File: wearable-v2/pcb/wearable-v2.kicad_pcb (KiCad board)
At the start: 2 copper layers, 89 parts, among them IC1 TESEO-LIV3F, J7 USB_C_Receptacle_USB2.0, SW1 SW_Push, U1 DT1446-04V, U10 ATmega328PB-M, U11 TMP1075, U12 MAX30102, U14 LIS2DE12, U2 MCP73832-2-OT, U3 TCA6408A, U4 FT201XQ, U6 BC833, U7 MX25R8035FZxxx0, U8 PCF85063ATL, U9 APDS-9250, Y1 32.768kHz

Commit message: Standard connector almost complete
Added JLCPCB manufacturer settings to PCB
Ensured all components are available and Tape and Reel with smallest footprint available
Signed-off-by: Adam Fowler <adam@adamfowler.org>
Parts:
- removed C22, C23: 1uF, Capacitor_SMD:C_0402_1005Metric
- removed C3: 4.7uF, Capacitor_SMD:C_0402_1005Metric
- removed the C6 at (115.1, 116.8)
- removed C7: 10uF, Capacitor_SMD:C_0402_1005Metric
- removed R3: 0, Resistor_SMD:R_0603_1608Metric
- removed TP4: VDD, TestPoint:TestPoint_Pad_D1.0mm
- U2: value MCP73832-2-OT -> MCP73831/2-2MC; footprint Package_TO_SOT_SMD:SOT-23-5 -> Package_DFN_QFN:DFN-8-1EP_3x2mm_P0.5mm_EP1.75x1.45mm
- moved H1 49.9 mm to (63.4, 40.1)
- moved SW1 46.9 mm to (58.8, 150.7), turned to 90 degrees
- moved C29 34.1 mm to (220.0, 84.9)
- moved TP18 34.1 mm to (229.1, 68.9)
- moved U14 34.1 mm to (222.8, 71.2)
- moved C27 34.1 mm to (219.5, 77.4)
- moved C28 34.1 mm to (222.3, 80.1)
- moved R7 34.1 mm to (221.8, 67.9)
- moved TP17 34.1 mm to (226.8, 76.3)
- moved R15 26.4 mm to (28.6, 126.6)
- moved C14 26.4 mm to (28.5, 122.8)
- moved U9 26.4 mm to (28.6, 124.7)
- moved C2 25.3 mm to (104.8, 131.3)
- moved C1 22.5 mm to (104.8, 132.3)
- moved U1 7.46 mm to (104.9, 135.8), turned to 90 degrees
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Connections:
- C10 pad 1: VDD1 -> VDD
- C11 pad 1: VDD1 -> VDD
- C12 pad 2: VDD1 -> VDD
- C13 pad 1: VDD1 -> VDD
- C24 pad 1: VDD1 -> VDD
- C30 pad 2: VDD1 -> VDD
- C6 pad 1: VDD1 -> VDD
- D2 pad 1: VDD1 -> VDD
- IC1 pad 14: VDD1 -> VDD
- IC1 pad 6: VDD1 -> VDD
- IC1 pad 7: VDD1 -> VDD
- IC1 pad 8: VDD1 -> VDD
- R1 pad 1: Net-(U2-PROG) -> GND
- R1 pad 2: GND -> Net-(U2-PROG)
- R10 pad 1: VDD1 -> VDD
- R11 pad 1: VDD1 -> VDD
- R16 pad 1: VDD1 -> VDD
- TP12 pad 1: VDD1 -> VDD
- U10 pad 18: VDD1 -> VDD
- U10 pad 4: VDD1 -> VDD
- U15 pad 11: (no net) -> GND
- U15 pad 8: VDD1 -> VDD
- U2 pad 1: /Standard Connector/CH_STAT -> VBUS
- U2 pad 2: GND -> VBUS
- U2 pad 4: VBUS -> +BATT
- U2 pad 5: Net-(U2-PROG) -> /Standard Connector/CH_STAT
- U3 pad 1: VDD1 -> VDD
- U3 pad 16: VDD1 -> VDD
- U3 pad 2: VDD1 -> VDD
- U4 pad 10: VDD1 -> VDD
- U6 pad 1: VDD1 -> VDD
- U7 pad 8: VDD1 -> VDD
- U8 pad 10: VDD1 -> VDD
- U8 pad EP: unconnected-(U8-PadEP) -> GND
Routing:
- net GND: track 35.6 -> 128.7 mm, vias 9 -> 17
- net VDD: track 0.00 -> 81.5 mm, vias 5 -> 6
- net +1V8: track 20.4 -> 70.8 mm, vias 0 -> 1
- net /Bio Board V1/SCL: track 44.4 -> 69.4 mm, vias 4 -> 5
- net VBUS: track 12.0 -> 32.0 mm, vias 0 -> 2
- net /Standard Connector/USB_D-: track 8.76 -> 23.0 mm, vias 2 -> 4
- net /Bio Board V1/SDA: track 58.2 -> 72.4 mm, vias 2 -> 7
- net /Standard Connector/USB_D+: track 3.99 -> 16.6 mm, vias 0 -> 2
- net /Compute - Fanstel BC833M - Nordic Semi nRF52833 based/LED_B: track 12.7 -> 3.08 mm
- net +BATT: track 25.1 -> 16.6 mm, vias 0 -> 2
- net VDD1: track 8.06 -> 0.00 mm
- net /Standard Connector/CH_STAT: track 7.48 -> 1.86 mm
- net /Compute - Fanstel BC833M - Nordic Semi nRF52833 based/SWDCLK: track 24.5 -> 21.0 mm
- net /Compute - Fanstel BC833M - Nordic Semi nRF52833 based/SWDIO: track 23.6 -> 21.4 mm
- net /Compute - Fanstel BC833M - Nordic Semi nRF52833 based/NFC2: track 8.72 -> 10.5 mm
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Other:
- board outline added: 247 x 147.3 mm
- board text added: "EXT 1 CPU TOP/CENTRAL"
- board text added: "EXT 1 CPU TOP/CENTRAL NB Components point DOWN (Toward Skin)"
- board text added: "EXT 2 BIO BOTTOM+SKIN"
- board text added: "EXT 3 GNSS/5G TOP/CENTRAL"
- board text added: "EXT 4 DISPLAY + FEEDBACK BOTTOM"
- board text added: "FRONT 1 LIGHT SENSOR TOP LEFT"
- board text added: "FRONT 2 GNSS ANTENNA TOP RIGHT"
- board text added: "FRONT 3 LEFT BUTTON BUTTOM LEFT"
- board text added: "FRONT 4 RIGHT BUTTON BUTTOM RIGHT"
- board text added: "TODO check USB-C D+ and D- and see if we need to connect both"
- board text removed: "8x40mm"
- board text removed: "Bio Board Here"
- board text removed: "Compute Board Here"
- board text removed: "Display Board Here"
- board text removed: "Front Button Panel"
- board text removed: "Front Light Sensor Panel"
- board text removed: "Positioning Board Here"

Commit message: Completed individual board layouts
Signed-off-by: Adam Fowler <adam@adamfowler.org>
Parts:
- TP10, TP11, TP8, U12: moved to B.Cu
- moved C21 193.7 mm to (215.9, 113.7), turned to 180 degrees
- moved C19 193.2 mm to (207.4, 106.5)
- moved C20 193.2 mm to (208.6, 106.5)
- moved U11 193.2 mm to (205.1, 106.8)
- moved C18 192.8 mm to (215.9, 112.7), turned to 180 degrees
- moved C17 191.8 mm to (216.0, 111.7), turned to 180 degrees
- moved U12 191.8 mm to (212.0, 111.7), turned to 180 degrees
- moved TP8 190.8 mm to (199.4, 107.0), turned to 180 degrees
- moved TP10 189.4 mm to (205.1, 112.3), turned to 180 degrees
- moved TP11 185.9 mm to (212.2, 107.4), turned to 180 degrees
- moved H1 166.4 mm to (218.2, 101.1)
- moved TP16 152.3 mm to (162.8, 124.1)
- moved TP15 140.8 mm to (160.3, 124.1)
- moved TP12 140.2 mm to (170.4, 124.1)
- moved TP13 139.7 mm to (167.9, 124.1)
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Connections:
- ANT1 pad 2: (no net) -> GND
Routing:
- net GND: track 128.7 -> 237.3 mm, vias 17 -> 20
- net /Bio Board V1/SDA: track 72.4 -> 143.3 mm, vias 7 -> 14
- net VDD: track 81.5 -> 151.7 mm, vias 6 -> 16
- net /Bio Board V1/SCL: track 69.4 -> 135.8 mm, vias 5 -> 11
- net /Positioning Board V1/GNSS_INT: track 0.00 -> 30.8 mm
- net /Positioning Board V1/POS_RESETn: track 0.00 -> 26.7 mm, vias 0 -> 2
- net /Compute - Fanstel BC833M - Nordic Semi nRF52833 based/EXT_INT1: track 0.00 -> 24.2 mm
- net +1V8: track 70.8 -> 87.2 mm, vias 1 -> 4
- net /Bio Board V1/BIO_INT: track 17.2 -> 3.34 mm
- net /Positioning Board V1/ANT_RF: track 0.00 -> 13.3 mm
- net Net-(ANT1-Pad1): track 0.00 -> 10.8 mm
- net /Positioning Board V1/ACC_INT1: track 0.00 -> 8.62 mm
- net /Positioning Board V1/ACC_INT2: track 0.00 -> 7.77 mm
- net Net-(U14-~{CS}): track 0.00 -> 3.78 mm
- net /Bio Board V1/TMP_INT: track 2.23 -> 4.87 mm, vias 0 -> 1
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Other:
- board size 247 x 147.3 mm -> 202.8 x 42.4 mm
- board text added: "EXT 1 COMPUTE TOP/CENTRAL NB Components point DOWN (Toward Skin) NB Connector points DOWN (Toward Skin and Connector board)"
- board text added: "EXT 2 BIO BOTTOM+SKIN NB Components point UP (Toward Connector) except Bio sensors which point DOWN (Toward skin) NB Connector points UP (Away from skin, toward Connector board)"
- board text added: "EXT 3 POSITIONING (GNSS), OR 5G, ETC. TOP/CENTRAL NB Components point DOWN (Toward Skin) NB Connector points DOWN (Toward Skin and Connector board)"
- board text added: "EXT 4 DISPLAY + FEEDBACK BOTTOM NB Components point UP (Toward Connector) Nothing points DOWN (Toward skin) NB Connector points UP (Away from skin, toward Connector board) NB ZIF connector extends out the bottom of this board and wraps around the top boards, then the battery, to connect to the display"
- board text removed: "35x19mm"
- board text removed: "ANT"
- board text removed: "Deleted???"
- board text removed: "EXT 1 CPU TOP/CENTRAL NB Components point DOWN (Toward Skin)"
- board text removed: "GNSS"
- board text removed: "TODO check USB-C D+ and D- and see if we need to connect both"
- board text removed: "TODO verify manufacturer track width minimums"

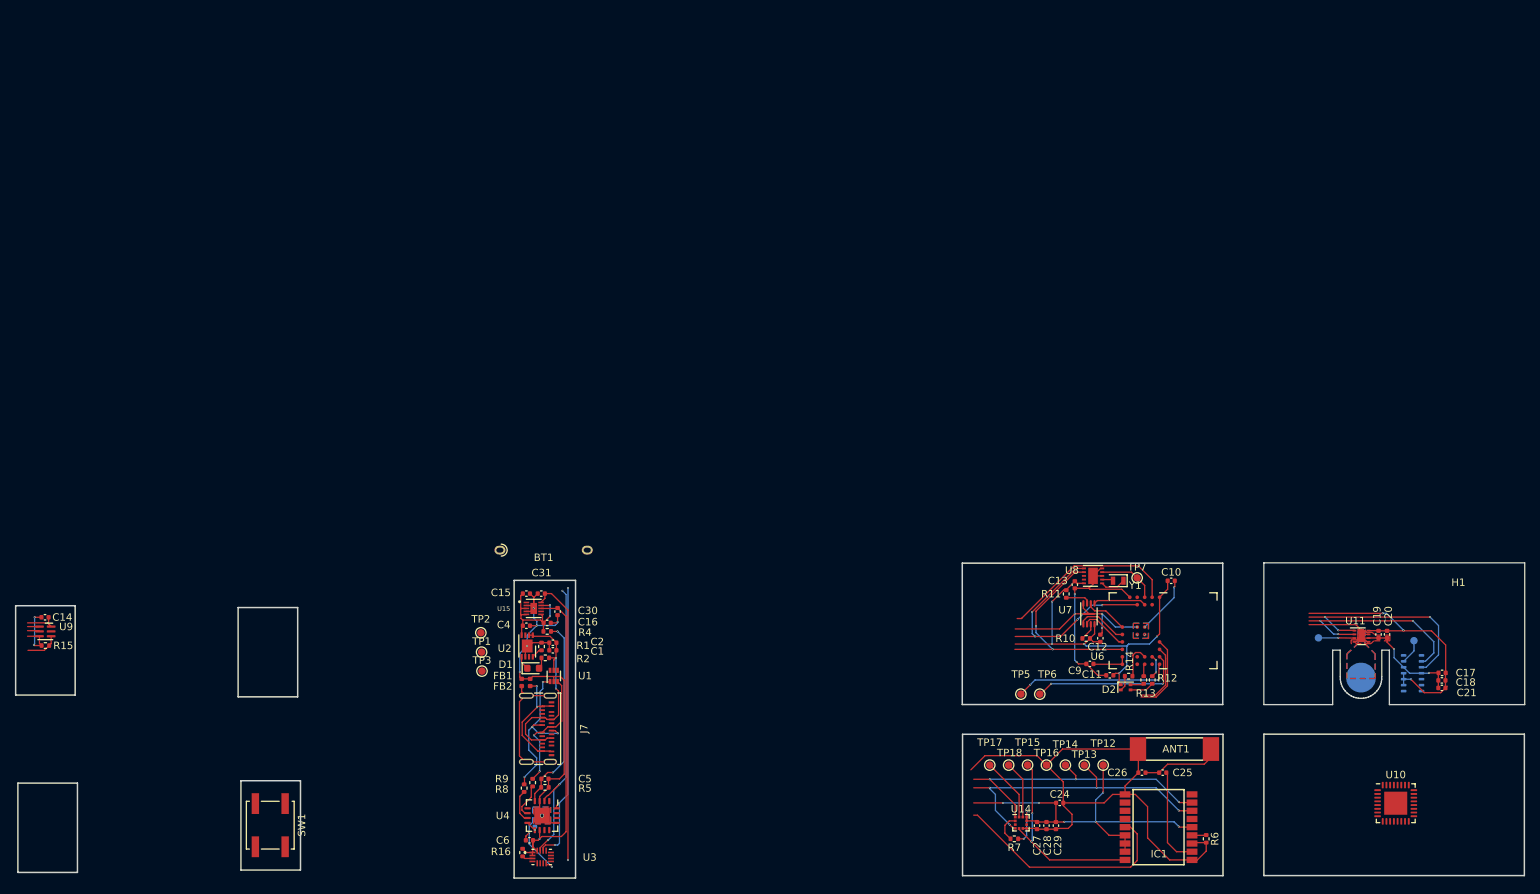
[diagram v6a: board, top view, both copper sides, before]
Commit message: Laid out all boards together
Added missing models for oscillator, push button, daylight sensor
Signed-off-by: Adam Fowler <adam@adamfowler.org>
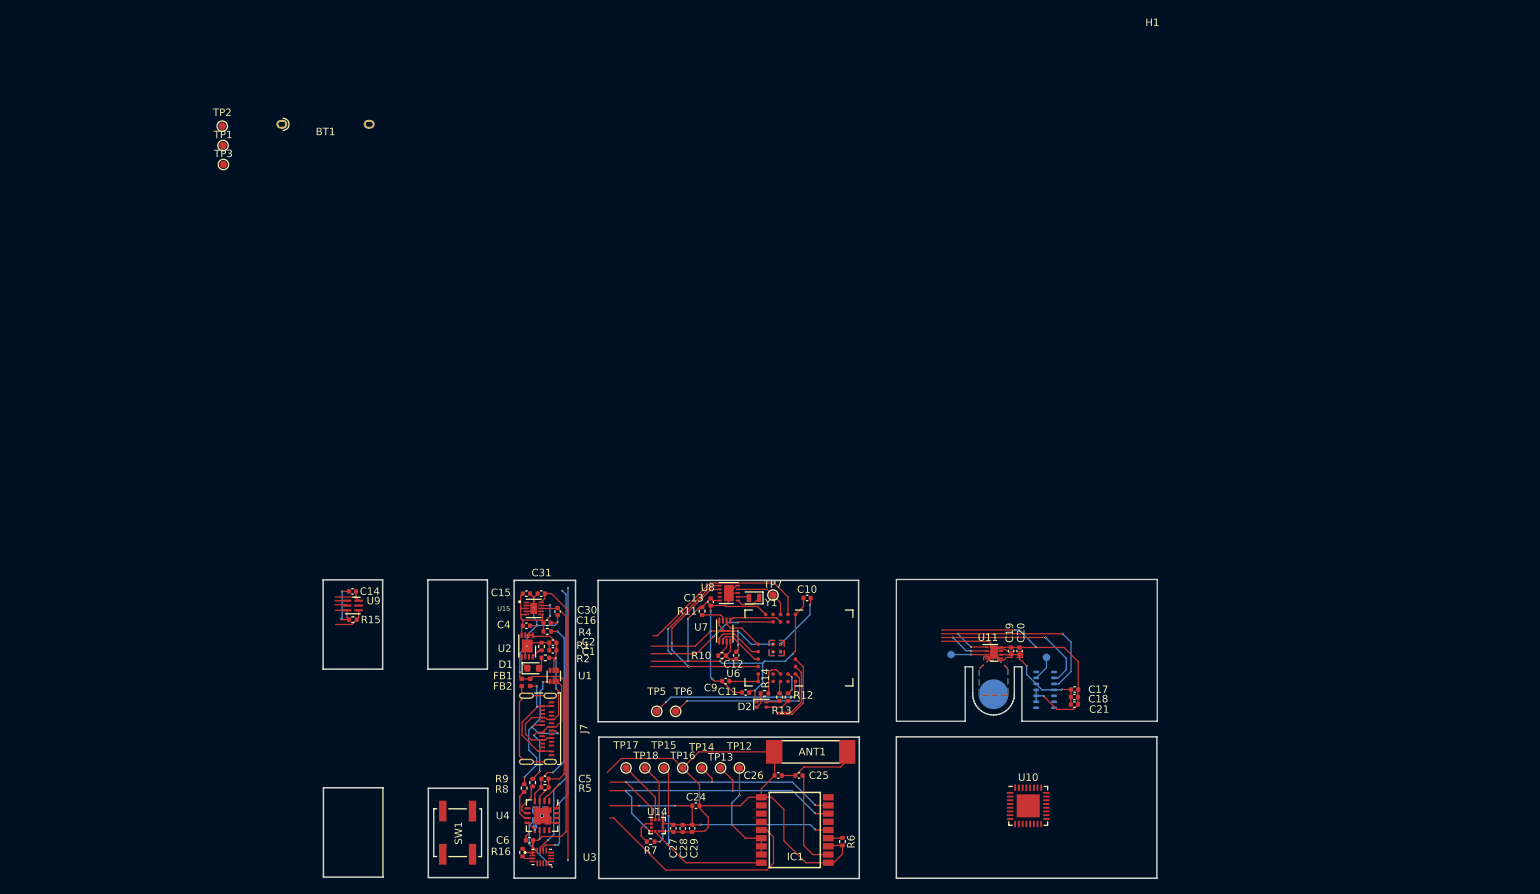
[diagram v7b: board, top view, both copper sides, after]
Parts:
- moved H1 85.7 mm to (177.0, 25.9)
- moved TP1 76.4 mm to (52.2, 40.8)
- moved TP2 76.4 mm to (52.1, 38.2)
- moved TP3 76.4 mm to (52.2, 43.4)
- moved BT1 64.3 mm to (65.9, 38.0)
- moved C17 49.4 mm to (166.6, 113.9)
- moved C19 49.4 mm to (158.1, 108.8)
- moved C20 49.4 mm to (159.2, 108.8)
- moved TP10 49.4 mm to (155.7, 114.6)
- moved TP11 49.4 mm to (162.8, 109.6)
- moved TP8 49.4 mm to (150.0, 109.2)
- moved U11 49.4 mm to (155.8, 109.0)
- moved U12 49.4 mm to (162.6, 114.0)
- moved C18 49.4 mm to (166.6, 114.9)
- moved C21 49.4 mm to (166.6, 116.0)
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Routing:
- net GND: track 237.3 -> 236.2 mm
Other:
- board size 202.8 x 42.4 mm -> 112.1 x 40.2 mm

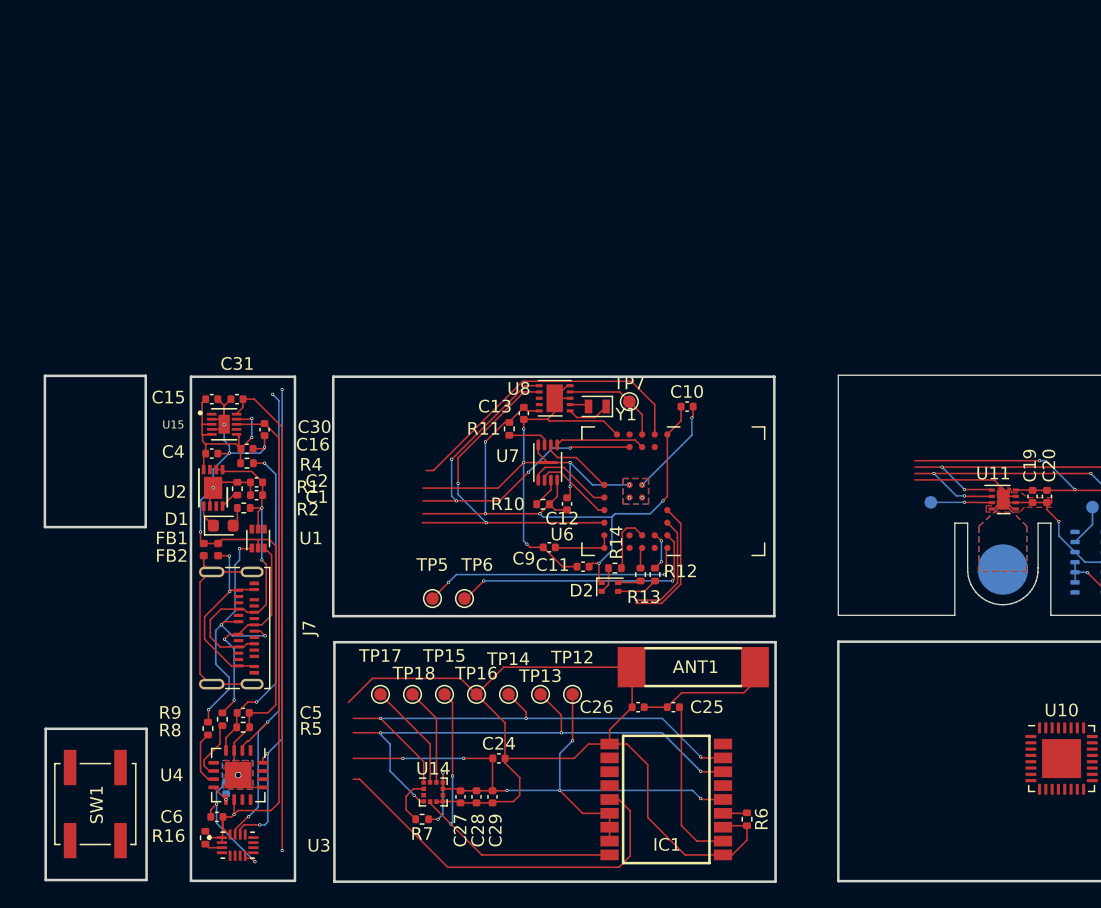
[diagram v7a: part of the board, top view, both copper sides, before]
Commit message: Added front connectors on main board
Signed-off-by: Adam Fowler <adam@adamfowler.org>
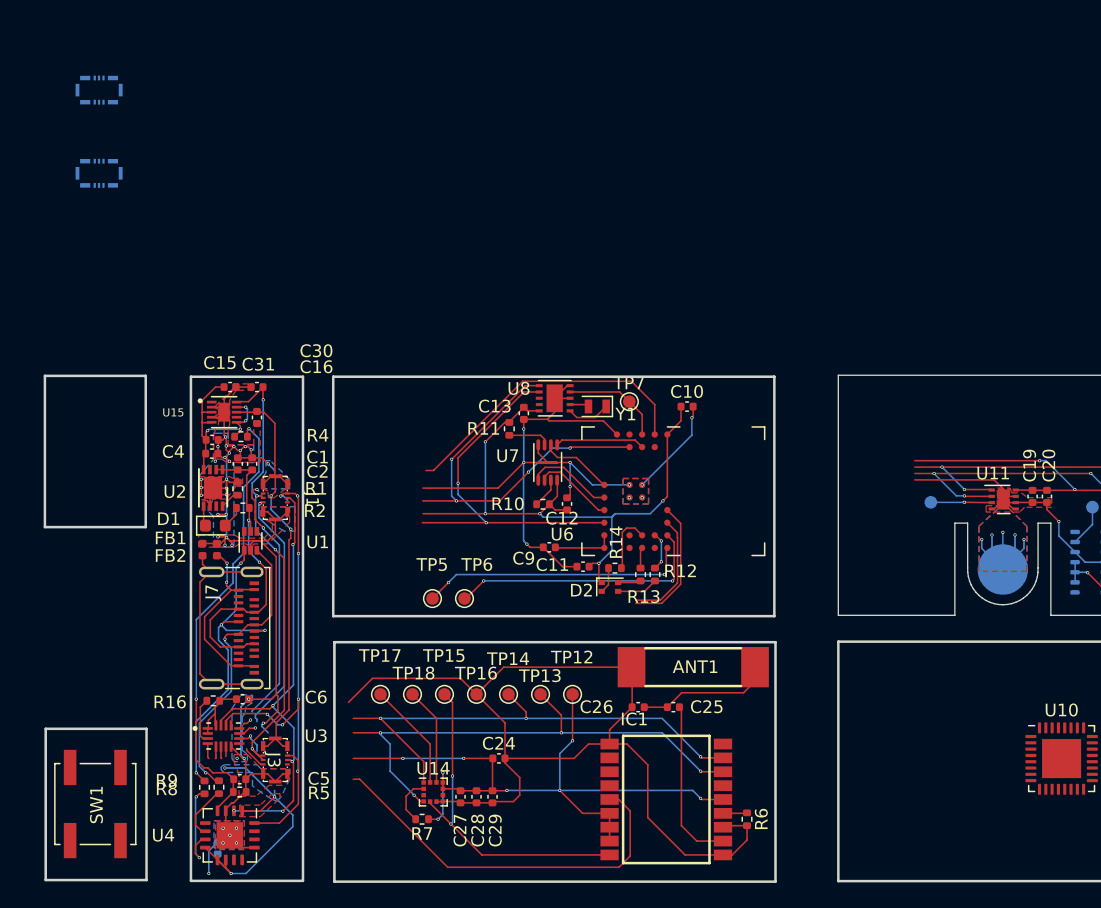
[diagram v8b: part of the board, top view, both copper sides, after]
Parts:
- added J1: HERALD_V2_CONN_RECEPTACLE, Herald:HERALD_V2_CONN_RECEPTACLE, F.Cu at (98.0, 108.9)
- added J2: HERALD_V2_CONN_RECEPTACLE, Herald:HERALD_V2_CONN_RECEPTACLE, B.Cu at (84.0, 76.5)
- added J3: HERALD_V2_CONN_RECEPTACLE, Herald:HERALD_V2_CONN_RECEPTACLE, F.Cu at (98.0, 129.7)
- added J4: HERALD_V2_CONN_RECEPTACLE, Herald:HERALD_V2_CONN_RECEPTACLE, B.Cu at (84.0, 83.1)
- TP12: value VDD1 -> VDD
- TP16: value GND1 -> GND
- U15: value ~ -> TLV751
- moved R16 10.9 mm to (93.0, 125.0), turned to 180 degrees
- moved C6 9.56 mm to (95.4, 124.8), turned to 0 degrees
- moved U3 8.73 mm to (93.9, 127.8)
- moved R9 5.40 mm to (93.5, 131.8)
- moved C5 5.27 mm to (95.2, 131.2)
- moved R5 5.14 mm to (95.2, 132.2)
- moved U4 4.83 mm to (94.4, 135.6)
- moved C8 4.83 mm to (93.4, 136.7)
- moved R8 4.67 mm to (92.4, 131.8)
- moved C16 2.85 mm to (93.0, 104.3)
- moved C1 2.51 mm to (96.1, 106.2), turned to -90 degrees
- moved R4 2.16 mm to (95.2, 104.0)
- moved C2 2.09 mm to (95.0, 106.2), turned to -90 degrees
- moved C31 1.85 mm to (96.5, 100.1)
- moved C15 1.74 mm to (94.4, 100.1)
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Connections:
- ANT1 pad 2: GND -> (no net)
- C14 pad 1: +1V8 -> VDD
- C17 pad 1: +1V8 -> VDD
- C18 pad 1: +1V8 -> VDD
- C19 pad 2: +1V8 -> VDD
- C20 pad 2: +1V8 -> VDD
- C21 pad 1: +1V8 -> VDD
- C31 pad 2: +1V8 -> 1V8
- C8 pad 1: Net-(U4-3V3OUT) -> VDD
- R15 pad 1: +1V8 -> VDD
- SW1 pad 1: +1V8 -> VDD
- U11 pad 8: +1V8 -> VDD
- U12 pad 10: +1V8 -> VDD
- U12 pad 11: +1V8 -> VDD
- U12 pad 9: +1V8 -> VDD
- U15 pad 10: +1V8 -> 1V8
- U4 pad 1: Net-(U4-3V3OUT) -> VDD
- U4 pad 8: Net-(U4-3V3OUT) -> VDD
- U4 pad 9: Net-(U4-3V3OUT) -> VDD
- U9 pad 3: +1V8 -> VDD
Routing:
- net +1V8: track 87.2 -> 0.00 mm, vias 4 -> 0
- net VDD: track 151.7 -> 219.8 mm, vias 16 -> 23
- net GND: track 236.2 -> 277.3 mm, vias 20 -> 51
- net 1V8: track 0.00 -> 37.3 mm, vias 0 -> 4
- net /Bio Board V1/INT_2: track 0.00 -> 22.4 mm, vias 0 -> 3
- net /Compute - Fanstel BC833M - Nordic Semi nRF52833 based/EXT_INT1: track 24.2 -> 43.8 mm, vias 0 -> 1
- net /Standard Connector/BT_STAT: track 26.1 -> 36.0 mm
- net /Standard Connector/USB_D+: track 16.6 -> 23.6 mm
- net /Standard Connector/USB_D-: track 23.0 -> 26.9 mm
- net /Positioning Board V1/GNSS_INT: track 30.8 -> 34.2 mm, vias 0 -> 1
- net Net-(U4-USBDM): track 4.43 -> 7.79 mm, vias 0 -> 2
- net /Bio Board V1/SDA: track 143.3 -> 139.9 mm, vias 14 -> 16
- net /Standard Connector/RST_CONN: track 1.44 -> 3.67 mm
- net /Bio Board V1/SCL: track 135.8 -> 138.0 mm, vias 11 -> 15
- net Net-(U4-3V3OUT): track 1.88 -> 0.00 mm, vias 1 -> 0
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- added copper zone on B.Cu, net VDD
- added copper zone on F.Cu, net VDD
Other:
- outline, holes or cut-outs redrawn
